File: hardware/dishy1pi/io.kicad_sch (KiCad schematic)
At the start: 34 parts, among them J3 TerminalBlock_9x2.54mm, J4 TerminalBlock_6x2.54mm, Q1 LTV-847S, U5 LTV827S-TA1, U6 LTV-847S, U7 LTV-827S-TA1, U8 LTV-817S-TA1

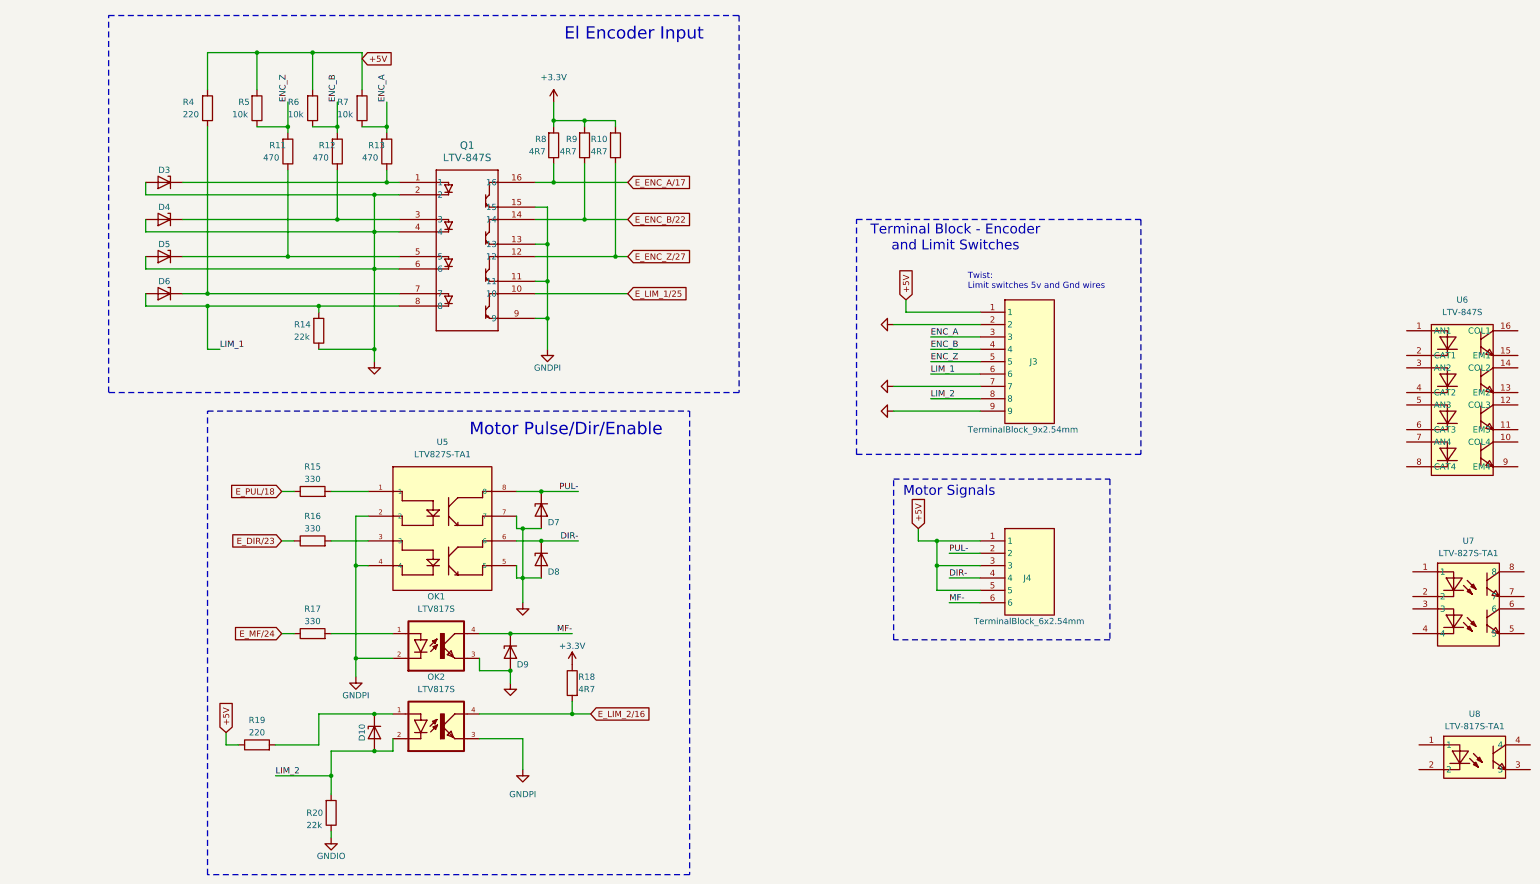
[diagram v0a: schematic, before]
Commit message: Parts place in PCB layout
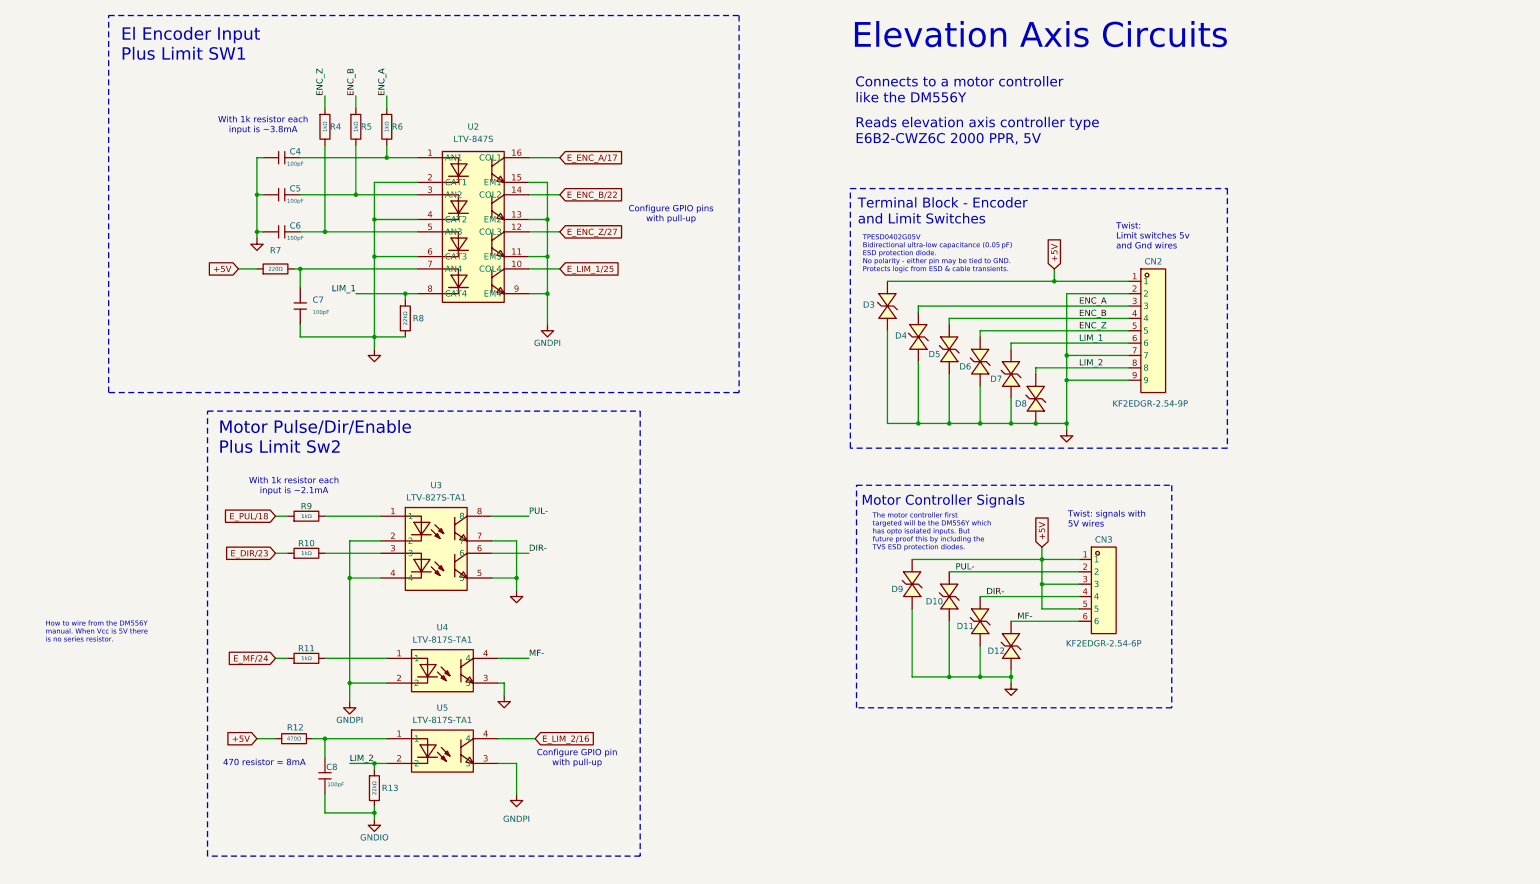
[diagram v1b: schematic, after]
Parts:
- removed D10, D3, D4, D5, D6, D7, D8, D9: TPESD0402G05V, Diode_SMD:D_0402_1005Metric, symbol Diode:PESD5V0L1UL
- removed J3: TerminalBlock_9x2.54mm, DishFootprints:TerminalBlock_9x2.54mm, symbol DishSympols:TerminalBlock_9x2.54mm
- removed J4: TerminalBlock_6x2.54mm, DishFootprints:TerminalBlock_6x2.54mm, symbol DishSympols:TerminalBlock_6x2.54mm
- removed OK1, OK2: LTV817S, DishFootprints:LTV817S, symbol DishSympols:LTV817S
- removed Q1: LTV-847S, DishFootprints:LTV847S, symbol DishSympols:ACPL-847-300E
- removed R10, R18, R8, R9: 4R7, Resistor_SMD:R_0402_1005Metric, symbol Device:R
- removed R11, R12, R13: 470, Resistor_SMD:R_0402_1005Metric, symbol Device:R
- removed R14, R20: 22k, Resistor_SMD:R_0402_1005Metric, symbol Device:R
- removed R15, R16, R17: 330, Resistor_SMD:R_0402_1005Metric, symbol Device:R
- removed R19, R4: 220, Resistor_SMD:R_0402_1005Metric, symbol Device:R
- removed R5, R6, R7: 10k, Resistor_SMD:R_0402_1005Metric, symbol Device:R
- removed U5: LTV827S-TA1, DishFootprints:LTV827S, symbol DishSympols:LTV827S-TA1
- removed U7: LTV-827S-TA1, MyParts:SMD-8_L9.8-W6.6-P2.54-LS10.3-BL, symbol MyParts:LTV-827S-TA1
- removed U8: LTV-817S-TA1, MyParts:OPTO-SMD-4_L4.6-W6.5-P2.54-LS10.3-BL, symbol MyParts:LTV-817S-TA1
- added C4, C5, C6, C7, C8: 100pF, PCM_JLCPCB:C_0402, symbol PCM_JLCPCB-Capacitors:0402,100pF
- added CN2: KF2EDGR-2.54-9P, MyParts:CONN-TH_9P-P2.54_KF2EDGR-2.54-9P, symbol MyParts:KF2EDGR-2.54-9P
- added CN3: KF2EDGR-2.54-6P, MyParts:CONN-TH_KF2EDGR-2.54-6P, symbol MyParts:KF2EDGR-2.54-6P
- added D10, D11, D12, D3, D4, D5, D6, D7, D8, D9: TPESD0402G05V, MyParts:D0402-BI, symbol MyParts:TPESD0402G05V
- added R10, R11, R4, R5, R6, R9: 1kΩ, PCM_JLCPCB:R_0402, symbol PCM_JLCPCB-Resistors:0402,1kΩ
- added R12: 470Ω, PCM_JLCPCB:R_0402, symbol PCM_JLCPCB-Resistors:0402,470Ω
- added R13, R8: 22kΩ, PCM_JLCPCB:R_0402, symbol PCM_JLCPCB-Resistors:0402,22kΩ
- added R7: 220Ω, PCM_JLCPCB:R_0402, symbol PCM_JLCPCB-Resistors:0402,220Ω
- added U3: LTV-827S-TA1, MyParts:LTV827S-TA1, symbol MyParts:LTV-827S-TA1
- added U4, U5: LTV-817S-TA1, MyParts:LTV817S, symbol MyParts:LTV-817S-TA1
- U2: renamed from U6; footprint MyParts:SMD-16_L20.0-W6.5-P2.54-LS10.2-BL -> myparts:SMD-16_L20.0-W6.5-P2.54-LS10.2-BL
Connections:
- net +5V: now also CN2.1, CN3.1, CN3.3, CN3.5, D3.1 (K), D9.1 (K), R12.1, R7.1
- net DIR-: now also CN3.4, D11.1 (K), U3.6
- net ENC_A: now also CN2.3, D4.1 (K), R6.1
- net ENC_B: now also CN2.4, D5.1 (K), R5.1
- net ENC_Z: now also CN2.5, D6.1 (K), R4.1
- net E_DIR/23: now also R10.1
- net E_ENC_A/17: now also U2.16 (COL1)
- net E_ENC_B/22: now also U2.14 (COL2)
- net E_ENC_Z/27: now also U2.12 (COL3)
- net E_LIM_1/25: now also U2.10 (COL4)
- net E_LIM_2/16: now also U5.4
- net E_MF/24: now also R11.1
- net E_PUL/18: now also R9.1
- net GNDIO: now also U2.2 (CAT1), U2.4 (CAT2), U2.6 (CAT3), C4.1, C5.1, C6.1, C7.2, C8.2, CN2.2, CN2.7, CN2.9, D10.2 (A), D11.2 (A), D12.2 (A), D3.2 (A), D4.2 (A), D5.2 (A), D6.2 (A), D7.2 (A), D8.2 (A), D9.2 (A), R13.2, R8.2, U3.5, U3.7, U4.3
- net GNDPI: now also U2.11 (EM3), U2.13 (EM2), U2.15 (EM1), U2.9 (EM4), U3.2, U3.4, U4.2, U5.3
- net LIM_1: now also U2.8 (CAT4), CN2.6, D7.1 (K), R8.1
- net LIM_2: now also CN2.8, D8.1 (K), R13.1, U5.2
- net MF-: now also CN3.6, D12.1 (K), U4.4
- net PUL-: now also CN3.2, D10.1 (K), U3.8
- net at U2.1 (AN1): now also C4.2, R6.2
- net at U2.3 (AN2): now also C5.2, R5.2
- net at U2.5 (AN3): now also C6.2, R4.2
- net at U2.7 (AN4): now also C7.1, R7.2
- new net: R11.2, U4.1
- new net: C8.1, R12.2, U5.1
- new net: R10.2, U3.3
- new net: R9.2, U3.1
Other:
- note added: "470 resistor = 8mA"
- note added: "Configure GPIO pin with pull-up"
- note added: "Configure GPIO pins with pull-up"
- note added: "Connects to a motor controller like the DM556Y"
- note added: "El Encoder Input Plus Limit SW1"
- note added: "Elevation Axis Circuits"
- note added: "How to wire from the DM556Y manual. When Vcc is 5V there is no series resistor."
- note added: "Motor Controller Signals"
- note added: "Motor Pulse/Dir/Enable Plus Limit Sw2"
- note added: "Reads elevation axis controller type E6B2-CWZ6C 2000 PPR, 5V"
- note added: "TPESD0402G05V Bidirectional ultra-low capacitance (0.05 pF) ESD protection diode. No polarity - either pin may be tied to GND. Protects logic from ESD & cable transients."
- note added: "The motor controller first targeted will be the DM556Y which has opto isolated inputs. But future proof this by including the TVS ESD protection diodes."
- note added: "Twist: signals with 5V wires"
- note added: "With 1k resistor each input is ~2.1mA"
- note added: "With 1k resistor each input is ~3.8mA"
- note removed: "El Encoder Input"
- note removed: "Motor Pulse/Dir/Enable"
- note removed: "Motor Signals"
- company: (none) -> JRDish
- title: IO Circuitry -> Elevation Axis IO Circuitry
- moved on the sheet: U2

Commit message: Ground and Power planes placed
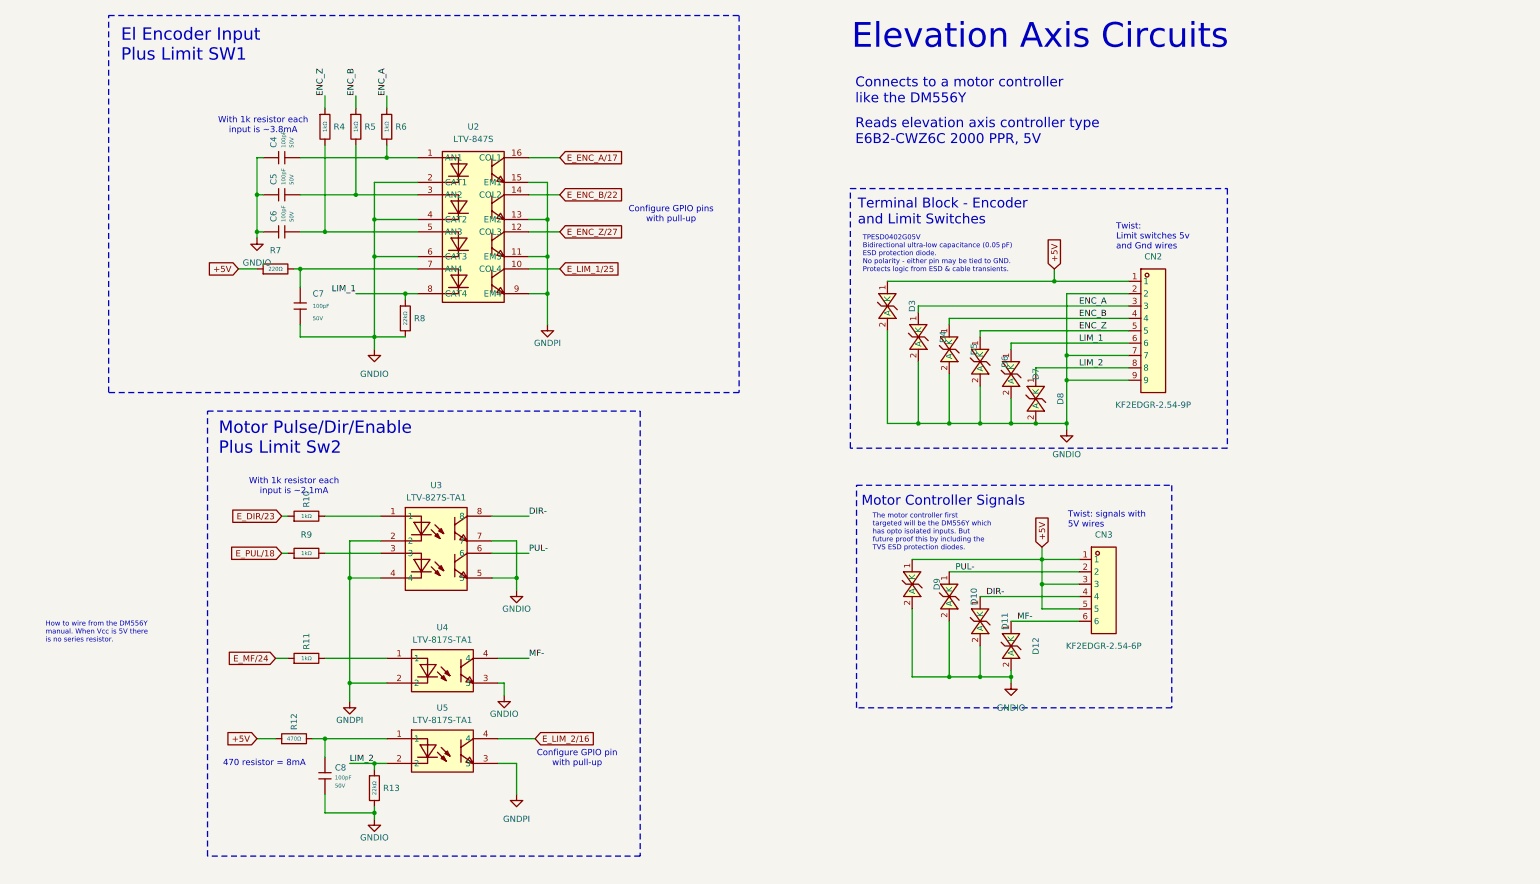
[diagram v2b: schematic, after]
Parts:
- U2: footprint myparts:SMD-16_L20.0-W6.5-P2.54-LS10.2-BL -> MyParts:SMD-16_L20.0-W6.5-P2.54-LS10.2-BL
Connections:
- net DIR-: now also U3.8; no longer U3.6
- net PUL-: now also U3.6; no longer U3.8
- net at R10.2: now also U3.1; no longer U3.3
- net at R9.2: now also U3.3; no longer U3.1
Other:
- moved on the sheet: R10

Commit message: Modifications based on first board assembly
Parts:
- removed C4, C5, C6, C8: 100pF, PCM_JLCPCB:C_0402, symbol PCM_JLCPCB-Capacitors:0402,100pF
- removed R5: 1kΩ, PCM_JLCPCB:R_0402, symbol PCM_JLCPCB-Resistors:0402,1kΩ
- added R5, R7, R9: 10kΩ, PCM_JLCPCB:R_0402, symbol PCM_JLCPCB-Resistors:0402,10kΩ
- added R8: 1kΩ, PCM_JLCPCB:R_0402, symbol PCM_JLCPCB-Resistors:0402,1kΩ
- renumbered C7 to C4, R7 to R10, R8 to R11, R10 to R12, R9 to R13, R11 to R14, R12 to R15, R13 to R16
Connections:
- net +5V: now also R16.2, R4.1, R6.1, R5.1, R7.1, R8.1, R9.1
- net ENC_A: now also U2.2 (CAT1), R9.2; no longer R6.1
- net ENC_B: now also U2.4 (CAT2), R7.2
- net ENC_Z: now also U2.6 (CAT3), R5.2; no longer R4.1
- net GNDIO: no longer R16.2, U2.2 (CAT1), U2.4 (CAT2), U2.6 (CAT3)
- net at U2.1 (AN1): now also R8.2; no longer R6.2
- net at U2.3 (AN2): now also R6.2
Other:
- note added: "Limit switch is NC to Gnd, causing current to flow. When triggered the limit switch is floating and pin 2 is 5V, no current flows through LED."
- note removed: "With 1k resistor each input is ~3.8mA"

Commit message: Added power circuit to dishy schematic
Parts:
- removed D3: TPESD0402G05V, MyParts:D0402-BI, symbol MyParts:TPESD0402G05V
- added D34: SMBJ16A, PCM_JLCPCB:D_SMB, symbol PCM_JLCPCB-Diodes:TVS-Uni,SMBJ16A
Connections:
- net +5V: no longer CN2.1
- net GNDIO: now also D34.2
- new net 12V_PROT: CN2.1, D34.1
